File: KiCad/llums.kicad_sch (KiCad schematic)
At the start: 27 parts, among them J1 CONNECTOR_MOTOR, Q1 IRLZ44N, Q2 IRLZ44N, Q3 IRLZ44N, Q4 IRLZ44N, Q5 IRLZ44N, Q6 IRLZ44N, Q7 IRLZ44N, U1 LM2596S-5, U2 LM1117MP-3.3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

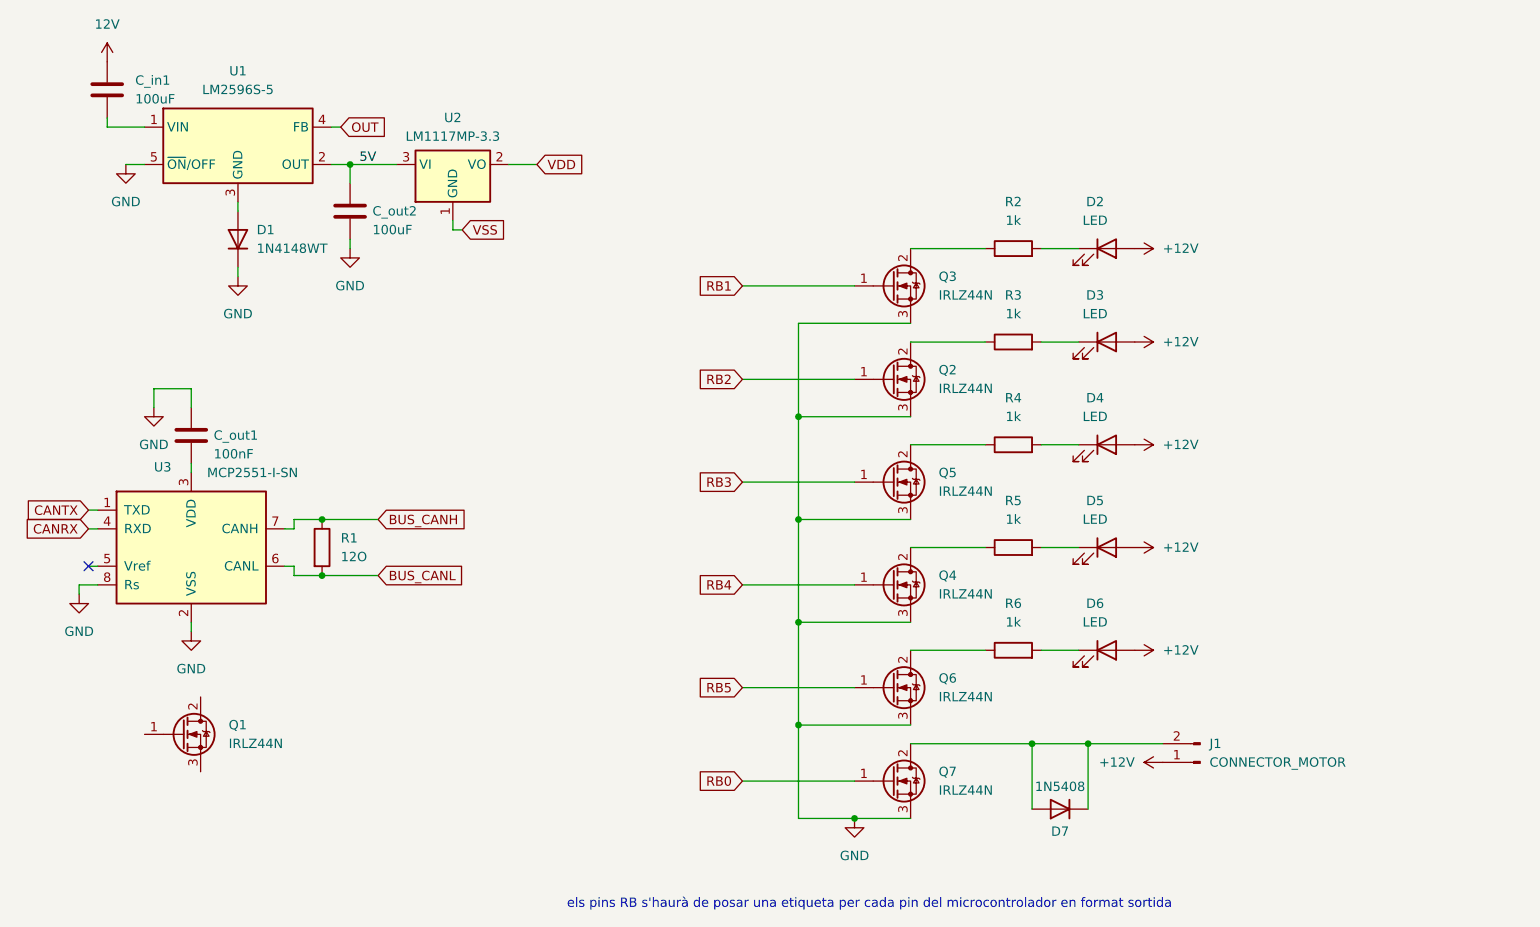
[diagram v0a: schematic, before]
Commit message: he canviat el micro
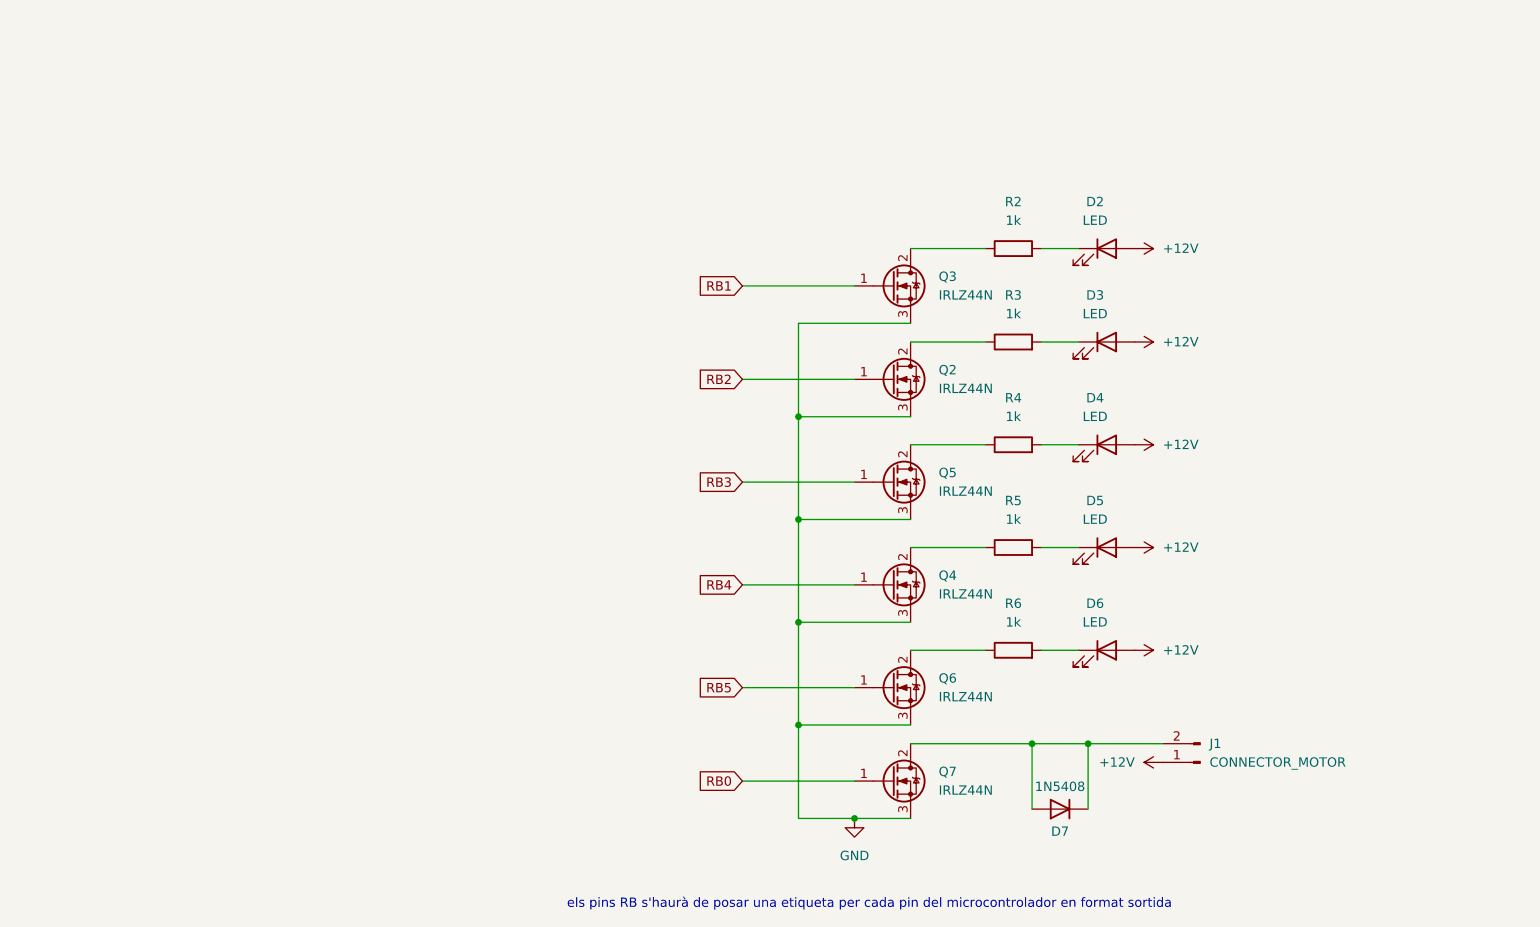
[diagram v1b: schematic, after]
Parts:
- removed C_in1, C_out2: 100uF, symbol Device:C
- removed C_out1: 100nF, symbol Device:C
- removed D1: 1N4148WT, Diode_SMD:D_SOD-523, symbol Diode:1N4148WT
- removed Q1: IRLZ44N, Package_TO_SOT_THT:TO-220-3_Vertical, symbol Transistor_FET:IRLZ44N
- removed R1: 12O, Relay_SMD:Relay_2P2T_10x6mm_TE_IMxxG, symbol Device:R
- removed U1: LM2596S-5, Package_TO_SOT_SMD:TO-263-5_TabPin3, symbol Regulator_Switching:LM2596S-5
- removed U2: LM1117MP-3.3, Package_TO_SOT_SMD:SOT-223-3_TabPin2, symbol Regulator_Linear:LM1117MP-3.3
- removed U3: MCP2551-I-SN, Package_SO:SOIC-8_3.9x4.9mm_P1.27mm, symbol Interface_CAN_LIN:MCP2551-I-SN
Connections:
- no-connect marks 1 -> 0

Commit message: ERC i footprints
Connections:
- net RB0 renamed NETEJA-FARS
- net RB1 renamed ENCREUAMENT
- net RB2 renamed CARRETERA
- net RB3 renamed DIURNA
- net RB4 renamed INTERM. ESQ
- net RB5 renamed INTERM. DRT
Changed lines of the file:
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@@
+	)
+	(junction
+		(at 170.18 55.88)
+		(diameter 0)
+		(color 0 0 0 0)
 	)
 	(junction
@@
 		)
 	)
-	(global_label "RB3"
+	(global_label "INTERM. DRT"
 		(shape input)
-		(at 116.84 87.63 180)
+		(at 116.84 115.57 180)
 		(fields_autoplaced yes)
 		(effects
@@
 		)
 		(property "Intersheetrefs" "${INTERSHEET_REFS}"
-			(at 110.1053 87.63 0)
+			(at 102.0015 115.57 0)
 			(effects
 				(font
@@
 		)
 	)
-	(global_label "RB1"
+	(global_label "INTERM. ESQ"
 		(shape input)
-		(at 116.84 60.96 180)
+		(at 116.84 101.6 180)
 		(fields_autoplaced yes)
 		(effects
@@
 		)
 		(property "Intersheetrefs" "${INTERSHEET_REFS}"
-			(at 110.1053 60.96 0)
+			(at 101.8201 101.6 0)
 			(effects
 				(font
@@
 		)
 	)
-	(global_label "RB2"
+	(global_label "NETEJA-FARS"
 		(shape input)
-		(at 116.84 73.66 180)
+		(at 116.84 128.27 180)
 		(fields_autoplaced yes)
 		(effects
@@
 		)
 		(property "Intersheetrefs" "${INTERSHEET_REFS}"
-			(at 110.1053 73.66 0)
+			(at 100.9734 128.27 0)
 			(effects
 				(font
@@
 		)
 	)
-	(global_label "RB5"
+	(global_label "DIURNA"
 		(shape input)
-		(at 116.84 115.57 180)
+		(at 116.84 87.63 180)
 		(fields_autoplaced yes)
 		(effects
@@
 		)
 		(property "Intersheetrefs" "${INTERSHEET_REFS}"
-			(at 110.1053 115.57 0)
+			(at 106.9604 87.63 0)
 			(effects
 				(font
@@
 		)
 	)
-	(global_label "RB4"
+	(global_label "ENCREUAMENT"
 		(shape input)
-		(at 116.84 101.6 180)
+		(at 116.84 60.96 180)
 		(fields_autoplaced yes)
 		(effects
@@
 		)
 		(property "Intersheetrefs" "${INTERSHEET_REFS}"
-			(at 110.1053 101.6 0)
+			(at 100.3687 60.96 0)
 			(effects
 				(font
@@
 		)
 	)
-	(global_label "RB0"
+	(global_label "CARRETERA"
 		(shape input)
-		(at 116.84 128.27 180)
+		(at 116.84 73.66 180)
 		(fields_autoplaced yes)
 		(effects
@@
 		)
 		(property "Intersheetrefs" "${INTERSHEET_REFS}"
-			(at 110.1053 128.27 0)
+			(at 103.332 73.66 0)
 			(effects
 				(font
@@
 					(unit 1)
 				)
+			)
+		)
+	)
+	(symbol
+		(lib_id "power:PWR_FLAG")
+		(at 170.18 55.88 0)
+		(unit 1)
+		(exclude_from_sim no)
+		(in_bom yes)
+		(on_board yes)
+		(dnp no)
+		(property "Reference" "#FLG04"
+			(at 170.18 53.975 0)
+			(effects
+				(font
+					(size 1.27 1.27)
+				)
+				(hide yes)
+			)
+		)
+		(property "Value" "PWR_FLAG"
+			(at 172.974 50.8 0)
+			(effects
+				(font
+					(size 1.27 1.27)
+				)
+			)
+		)
+		(property "Footprint" ""
+			(at 170.18 55.88 0)
+			(effects
+				(font
+					(size 1.27 1.27)
+				)
+				(hide yes)
+			)
+		)
+		(property "Datasheet" "~"
+			(at 170.18 55.88 0)
+			(effects
+				(font
+					(size 1.27 1.27)
+				)
+				(hide yes)
+			)
+		)
+		(property "Description" "Special symbol for telling ERC where power comes from"
+			(at 170.18 55.88 0)
+			(effects
+				(font
+					(size 1.27 1.27)
+				)
+				(hide yes)
+			)
+		)
+		(pin "1"
+		)
+		(instances
+			(project ""
+				(path "/b4874c87-978f-427f-bc45-3635f8629977/0edcf3aa-0722-4786-beaa-59b728b7a9fc"
+					(reference "#FLG04")
+					(unit 1)
+				)

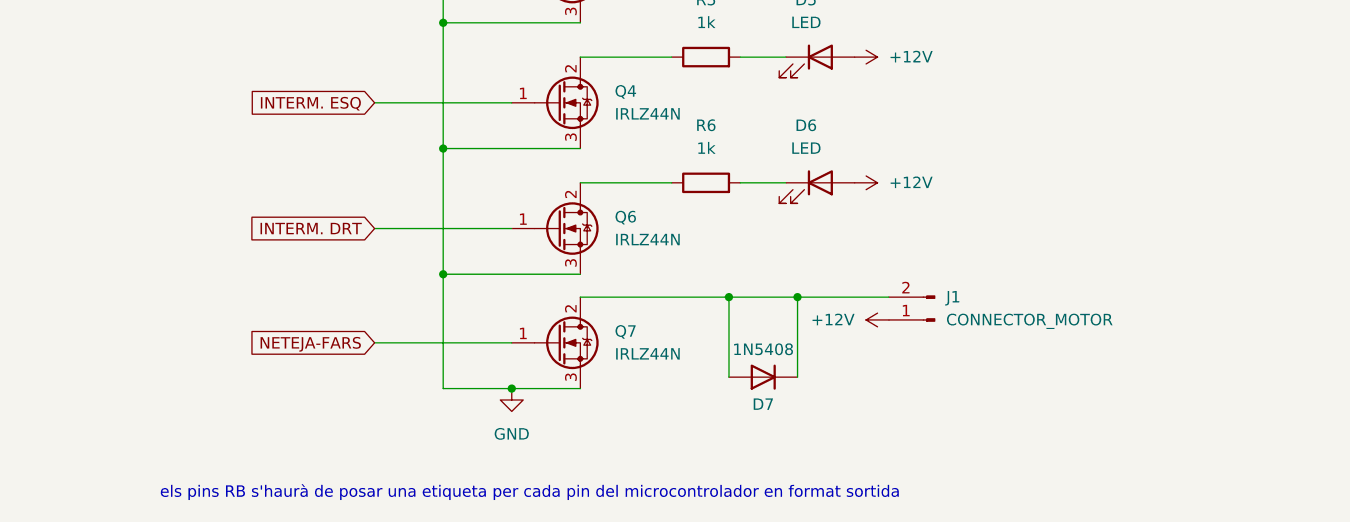
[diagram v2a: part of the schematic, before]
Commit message: relé fet
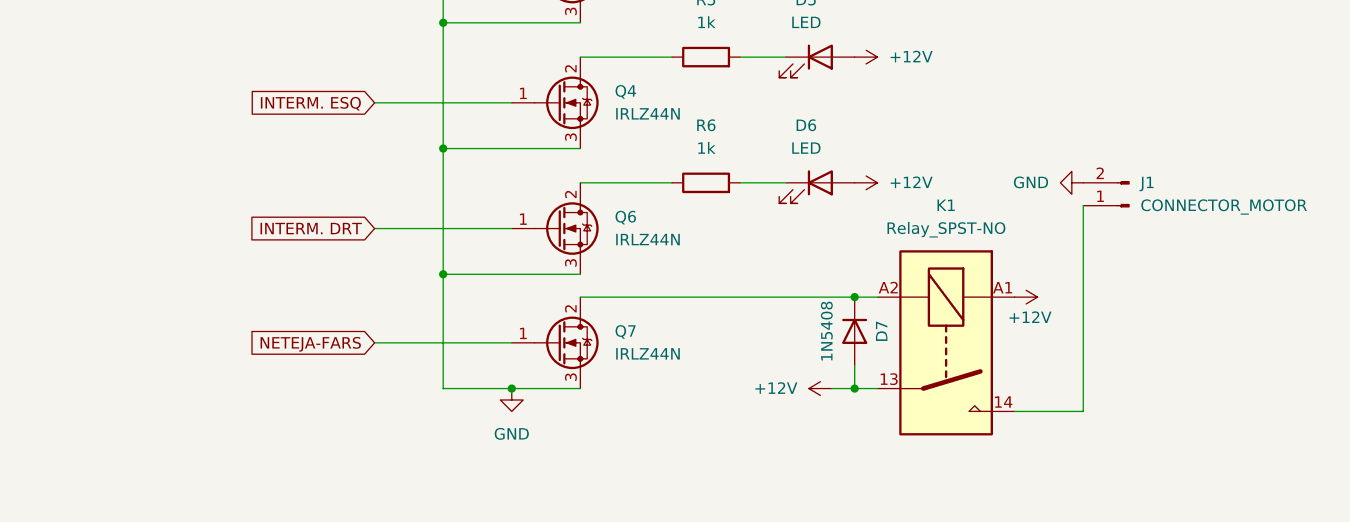
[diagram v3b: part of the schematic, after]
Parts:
- added K1: Relay_SPST-NO, symbol Relay:Relay_SPST-NO
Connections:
- net +12V: now also D7.2 (A), K1.13, K1.A1; no longer J1.1 (Pin_1)
- net GND: now also J1.2 (Pin_2)
- net at D7.1 (K), Q7.2 (D): now also K1.A2; no longer D7.2 (A), J1.2 (Pin_2)
- new net: J1.1 (Pin_1), K1.14
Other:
- note removed: "els pins RB s'haurà de posar una etiqueta per cada pin del microcontrolador en format sortida"
- moved on the sheet: D7, J1
